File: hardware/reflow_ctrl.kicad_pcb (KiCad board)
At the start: 2 copper layers, 160 x 100 mm, 36 parts, among them IC1 MAX6675, IC2 ATXMEGA128A4U-A, P1 PDI, U1 LT1129CST-3.3, U2 MOC3063, U3 BTA41/600B, X1 USB-Mini-B, X2 Mains, X3 Load, X4 Thermocouple

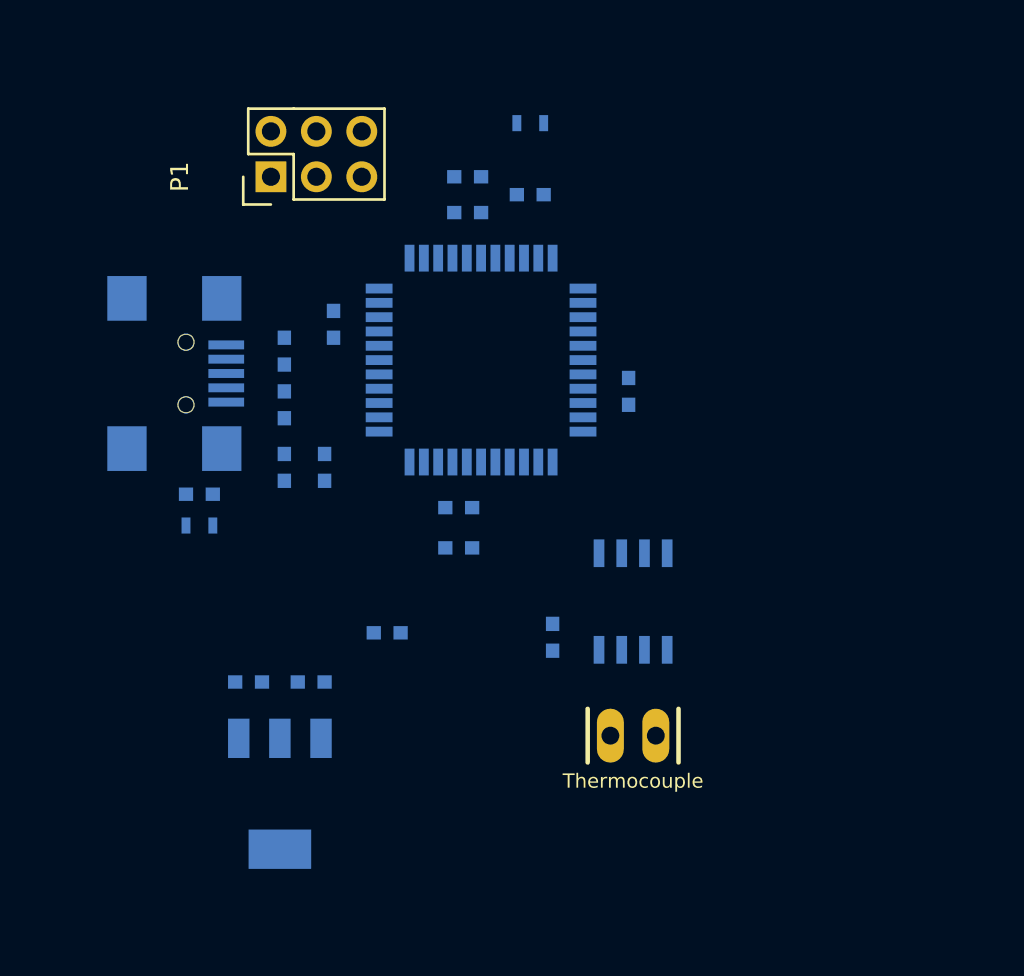
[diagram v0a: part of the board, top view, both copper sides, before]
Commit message: Use big USB-B THT connector
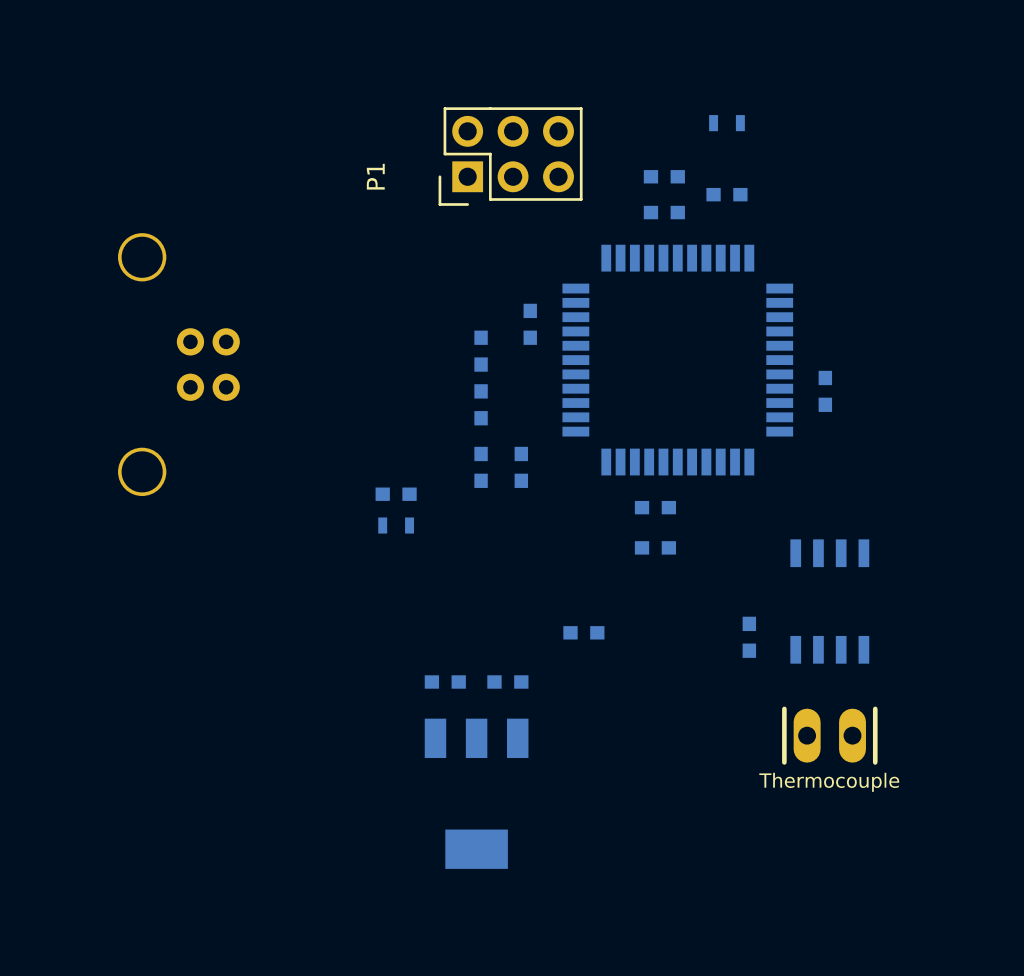
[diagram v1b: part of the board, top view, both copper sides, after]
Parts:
- X1: footprint uMIDI:USB-mini-B-UX60MB-5ST -> Connect:USB_B
- moved C1 11.0 mm to (82.5, 107.2)
- moved C10 11.0 mm to (97.5, 89.5)
- moved C11 11.0 mm to (102.2, 115.2)
- moved C2 11.0 mm to (85.2, 117.8)
- moved C3 11.0 mm to (89.5, 105.8)
- moved C4 11.0 mm to (97.0, 110.2)
- moved C5 11.0 mm to (88.8, 117.8)
- moved C6 11.0 mm to (106.5, 101.5)
- moved C7 11.0 mm to (97.0, 108.0)
- moved C8 11.0 mm to (90.0, 97.8)
- moved C9 11.0 mm to (97.5, 91.5)
- moved D1 11.0 mm to (87.2, 105.8)
- moved D2 11.0 mm to (87.2, 99.2)
- moved D3 11.0 mm to (87.2, 102.2)
- moved IC1 11.0 mm to (106.8, 113.2)
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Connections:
- net Net-(D2-Pad2) renamed /USB_n
- net Net-(D3-Pad2) renamed /USB_p
- X1 pad 4: (no net) -> GND
- X1 pad 5: GND -> Net-(C1-Pad1)

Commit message: Update board
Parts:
- removed C10, C4, C5, L1: 10u, Capacitors_SMD:C_0603
- removed C3, C6, C7, C8, C9: 100n, Capacitors_SMD:C_0603
- removed D1, D2, D3: TVS 5V, Capacitors_SMD:C_0603
- removed IC2: ATXMEGA128A4U-A, Housings_QFP:TQFP-44_10x10mm_Pitch0.8mm
- removed L2: Bead 1k@100MHz, Capacitors_SMD:C_0603
- removed P1: PDI, Pin_Headers:Pin_Header_Straight_2x03
- removed R1: 1M, Resistors_SMD:R_0603
- removed R2: 10k, Resistors_SMD:R_0603
- removed REF**: EuroBoard160mmX100mm_holes, EuroBoard_Outline:EuroBoard160mmX100mm_holes
- removed U1: LT1129CST-3.3, uMIDI:SOT-223
- C1: value 4.7n -> 100n
- C2: value 10u -> 100n
- X1: value USB-Mini-B -> Master; footprint Connect:USB_B -> uMIDI:Con-boxed_header-THT; moved to F.Cu
- moved X4 63.4 mm to (125.0, 60.0), turned to 180 degrees
- moved IC1 46.9 mm to (125.0, 70.0), turned to 270 degrees
- moved X1 36.9 mm to (108.7, 89.5), turned to 90 degrees
- moved C1 24.3 mm to (106.5, 111.2)
- moved C2 24.3 mm to (109.2, 121.8)
- moved X3 24.3 mm to (190.0, 75.0)
- moved X2 23.6 mm to (190.0, 100.0)
- moved F1 22.9 mm to (165.0, 112.5)
- moved C12 22.4 mm to (160.0, 77.8)
- moved R3 22.4 mm to (149.2, 100.8)
- moved R4 22.4 mm to (149.8, 82.0)
- moved R5 22.4 mm to (145.5, 71.0)
- moved R6 22.4 mm to (160.0, 83.0)
- moved U2 22.4 mm to (146.8, 91.5)
- moved U3 22.4 mm to (149.8, 76.2)
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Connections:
- C1 pad 1: Net-(C1-Pad1) -> +3V3
- C11 pad 1: +5V -> +3V3
- C2 pad 1: VBUS -> +3V3
- IC1 pad 4: +5V -> +3V3
- X1 pad 1: VBUS -> +3V3
- X1 pad 2: /USB_p -> (no net)
- X1 pad 3: /USB_n -> (no net)
- X1 pad 4: GND -> (no net)
- X1 pad 5: Net-(C1-Pad1) -> /TC_SO
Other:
- board outline removed

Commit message: Prepare net classes
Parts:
- moved F1 17.5 mm to (172.0, 96.5), turned to 270 degrees
- moved VR1 16.0 mm to (172.8, 72.0)
- moved C12 14.3 mm to (165.5, 64.5)
- moved R6 13.7 mm to (165.5, 70.5)
- moved X3 5.00 mm to (190.0, 70.0)
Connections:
- net Net-(C12-Pad1) renamed /Snub
- net Net-(F1-Pad1) renamed /L_main_fused
- net Net-(R4-Pad2) renamed /MOC_A1
- net Net-(R5-Pad1) renamed /MOC_A2
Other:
- net class AC added: clearance 1, trace_width 5, via_dia 1.5, via_drill 1
- net class AC-LC added: clearance 1, trace_width 0.3, via_dia 1.5, via_drill 1
- net class Default: clearance 0.2 -> 0.3; trace_width 0.25 -> 0.3; via_dia 0.6 -> 1.5; via_drill 0.4 -> 1
- rule trace_clearance: 0.2 -> 0.3

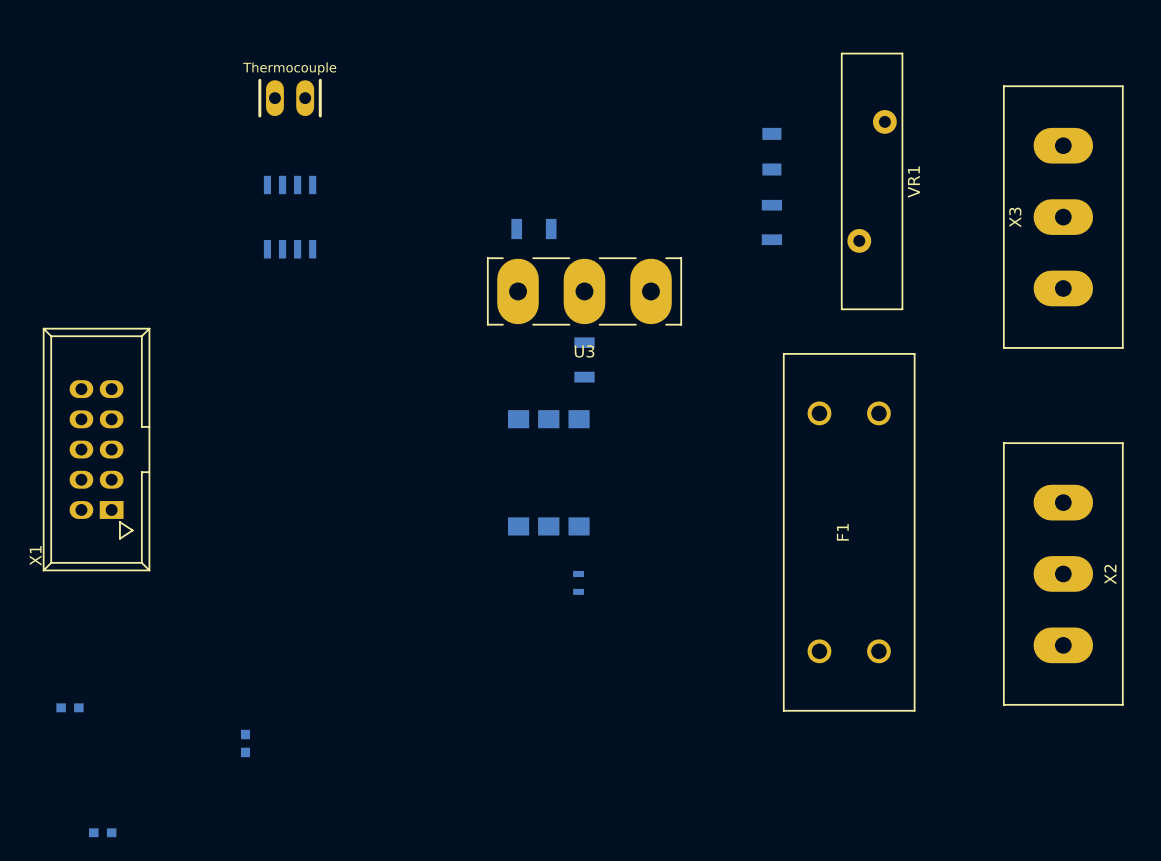
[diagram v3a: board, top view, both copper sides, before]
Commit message: Add mounting holes
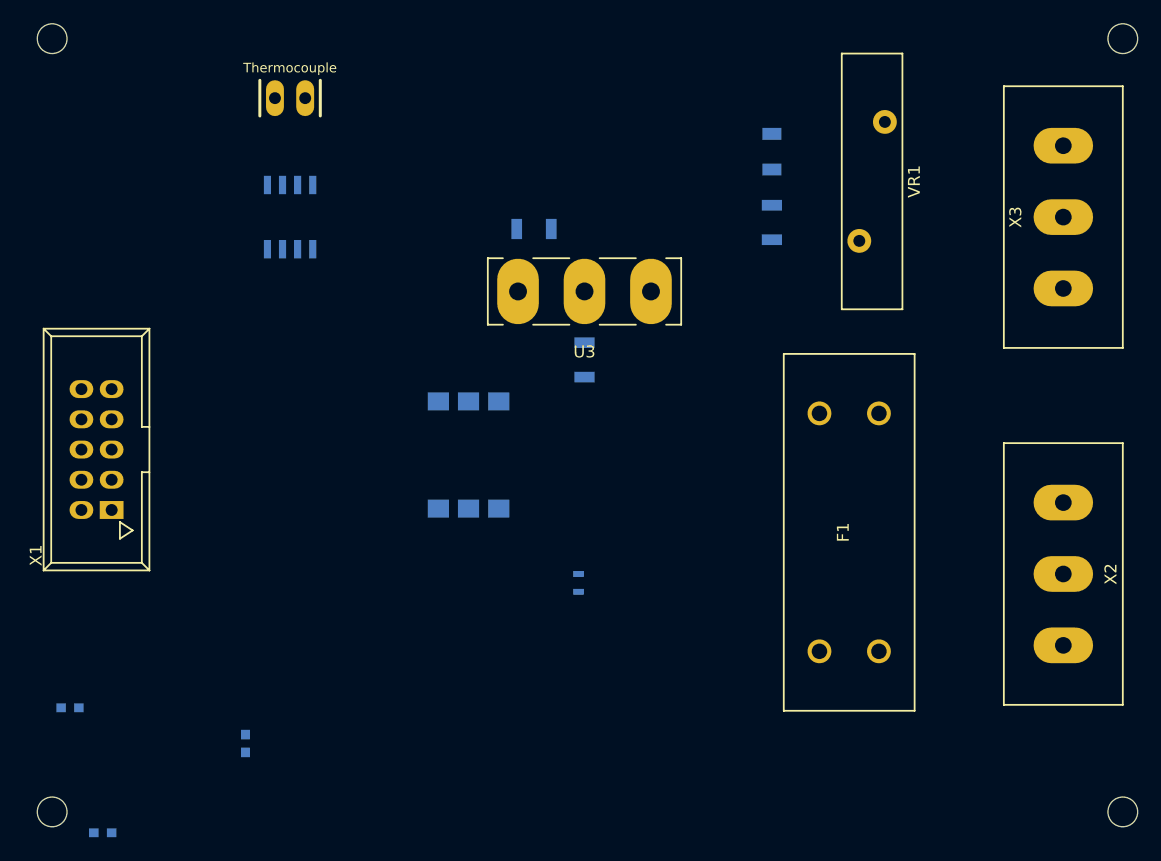
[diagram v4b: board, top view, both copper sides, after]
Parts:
- added REF**: MountingHole_2-5mm, Mounting_Holes:MountingHole_2-5mm, F.Cu at (195.0, 120.0)
- added REF**: MountingHole_2-5mm, Mounting_Holes:MountingHole_2-5mm, F.Cu at (105.0, 120.0)
- added REF**: MountingHole_2-5mm, Mounting_Holes:MountingHole_2-5mm, F.Cu at (105.0, 55.0)
- added REF**: MountingHole_2-5mm, Mounting_Holes:MountingHole_2-5mm, F.Cu at (195.0, 55.0)
- moved U2 6.91 mm to (140.0, 90.0)
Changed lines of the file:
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@@
 (kicad_pcb (version 4) (host pcbnew "(2015-09-12 BZR 6188)-product")
   (general
-    (links 33)
+    (links 0)
     (no_connects 33)
-    (area 99.899999 49.899999 200.100001 125.425)
+    (area 95.615476 49.075 213 132.700001)
     (thickness 1.6)
-    (drawings 4)
+    (drawings 6)
     (tracks 0)
     (zones 0)
-    (modules 17)
+    (modules 21)
     (nets 18)
   )
@@
     (add_net /Snub)
   )
+  (module Mounting_Holes:MountingHole_2-5mm (layer F.Cu)
+    (at 195 120)
+    (descr "Mounting hole, Befestigungsbohrung, 2,5mm, No Annular, Kein Restring,")
+    (tags "Mounting hole, Befestigungsbohrung, 2,5mm, No Annular, Kein Restring,")
+    (fp_text reference REF** (at 0 -3.50012) (layer F.SilkS) hide
+      (effects (font (size 1 1) (thickness 0.15)))
+    )
+    (fp_text value MountingHole_2-5mm (at 0 4) (layer F.Fab)
+      (effects (font (size 1 1) (thickness 0.15)))
+    )
+    (fp_circle (center 0 0) (end 2.5 0) (layer Cmts.User) (width 0.381))
+    (pad 1 thru_hole circle (at 0 0) (size 2.5 2.5) (drill 2.5) (layers))
+  )
+  (module Mounting_Holes:MountingHole_2-5mm (layer F.Cu)
+    (at 105 120)
+    (descr "Mounting hole, Befestigungsbohrung, 2,5mm, No Annular, Kein Restring,")
+    (tags "Mounting hole, Befestigungsbohrung, 2,5mm, No Annular, Kein Restring,")
+    (fp_text reference REF** (at 0 -3.50012) (layer F.SilkS) hide
+      (effects (font (size 1 1) (thickness 0.15)))
+    )
+    (fp_text value MountingHole_2-5mm (at 0 4) (layer F.Fab)
+      (effects (font (size 1 1) (thickness 0.15)))
+    )
+    (fp_circle (center 0 0) (end 2.5 0) (layer Cmts.User) (width 0.381))
+    (pad 1 thru_hole circle (at 0 0) (size 2.5 2.5) (drill 2.5) (layers))
+  )
+  (module Mounting_Holes:MountingHole_2-5mm (layer F.Cu)
+    (at 105 55)
+    (descr "Mounting hole, Befestigungsbohrung, 2,5mm, No Annular, Kein Restring,")
+    (tags "Mounting hole, Befestigungsbohrung, 2,5mm, No Annular, Kein Restring,")
+    (fp_text reference REF** (at 0 -3.50012) (layer F.SilkS) hide
+      (effects (font (size 1 1) (thickness 0.15)))
+    )
+    (fp_text value MountingHole_2-5mm (at 0 -4) (layer F.Fab)
+      (effects (font (size 1 1) (thickness 0.15)))
+    )
+    (fp_circle (center 0 0) (end 2.5 0) (layer Cmts.User) (width 0.381))
+    (pad 1 thru_hole circle (at 0 0) (size 2.5 2.5) (drill 2.5) (layers))
+  )
   (module Capacitors_SMD:C_0603 (layer B.Cu)
     (at 106.5 111.25 180)
@@
   )
   (module uMIDI:MOC3063_SMT (layer B.Cu)
-    (at 146.75 91.5 180)
+    (at 140 90 180)
     (fp_text reference U2 (at 0 -7 180) (layer B.SilkS)
       (effects (font (size 1 1) (thickness 0.15)) (justify mirror))
@@
       (net 1 GND))
   )
+  (module Mounting_Holes:MountingHole_2-5mm (layer F.Cu)
+    (at 195 55)
+    (descr "Mounting hole, Befestigungsbohrung, 2,5mm, No Annular, Kein Restring,")
+    (tags "Mounting hole, Befestigungsbohrung, 2,5mm, No Annular, Kein Restring,")
+    (fp_text reference REF** (at 0 -3.50012) (layer F.SilkS) hide
+      (effects (font (size 1 1) (thickness 0.15)))
+    )
+    (fp_text value MountingHole_2-5mm (at 0 -4) (layer F.Fab)
+      (effects (font (size 1 1) (thickness 0.15)))
+    )
+    (fp_circle (center 0 0) (end 2.5 0) (layer Cmts.User) (width 0.381))
+    (pad 1 thru_hole circle (at 0 0) (size 2.5 2.5) (drill 2.5) (layers))
+  )
+  (dimension 75 (width 0.3) (layer Dwgs.User)
+    (gr_text "75.000 mm" (at 206.35 87.5 90) (layer Dwgs.User)
+      (effects (font (size 1.5 1.5) (thickness 0.3)))
+    )
+    (feature1 (pts (xy 200 50) (xy 207.7 50)))
+    (feature2 (pts (xy 200 125) (xy 207.7 125)))
+    (crossbar (pts (xy 205 125) (xy 205 50)))
+    (arrow1a (pts (xy 205 50) (xy 205.586421 51.126504)))
+    (arrow1b (pts (xy 205 50) (xy 204.413579 51.126504)))
+    (arrow2a (pts (xy 205 125) (xy 205.586421 123.873496)))
+    (arrow2b (pts (xy 205 125) (xy 204.413579 123.873496)))
+  )
+  (dimension 100 (width 0.3) (layer Dwgs.User)
+    (gr_text "100.000 mm" (at 150 131.35) (layer Dwgs.User)
+      (effects (font (size 1.5 1.5) (thickness 0.3)))
+    )
+    (feature1 (pts (xy 200 125) (xy 200 132.7)))
+    (feature2 (pts (xy 100 125) (xy 100 132.7)))
+    (crossbar (pts (xy 100 130) (xy 200 130)))
+    (arrow1a (pts (xy 200 130) (xy 198.873496 130.586421)))
+    (arrow1b (pts (xy 200 130) (xy 198.873496 129.413579)))
+    (arrow2a (pts (xy 100 130) (xy 101.126504 130.586421)))
+    (arrow2b (pts (xy 100 130) (xy 101.126504 129.413579)))
+  )
   (gr_line (start 100 125) (end 100 50) (layer Margin) (width 0.2))

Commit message: Disentangle connector pinout; Start placement
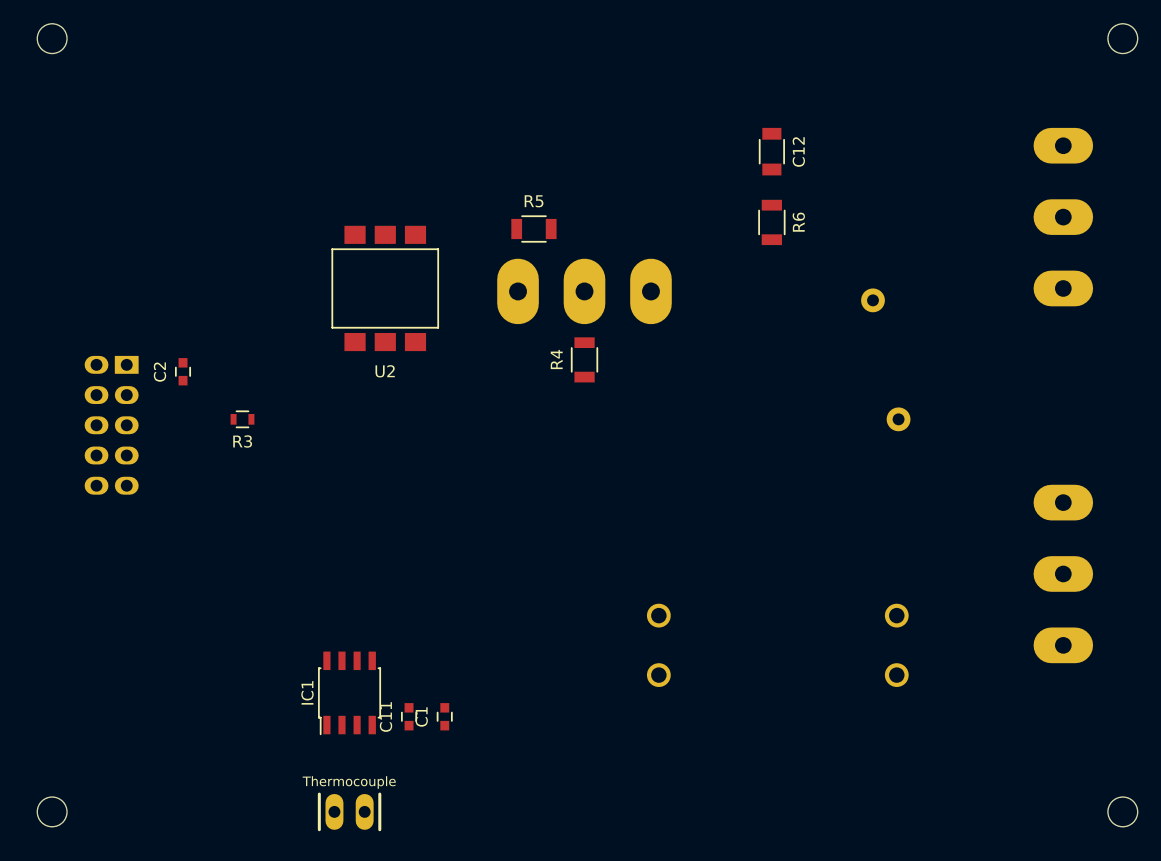
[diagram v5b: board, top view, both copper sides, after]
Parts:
- C1, C11, C12, C2, IC1, R3, R4, R5, R6, U2: moved to F.Cu
- F1, U3, VR1, X1, X2, X3: moved to B.Cu
- moved X4 60.2 mm to (130.0, 120.0)
- moved IC1 40.3 mm to (130.0, 110.0), turned to 90 degrees
- moved C2 39.3 mm to (116.0, 83.0), turned to 90 degrees
- moved C1 31.5 mm to (138.0, 112.0), turned to 90 degrees
- moved R3 31.4 mm to (121.0, 87.0), turned to 180 degrees
- moved U2 15.7 mm to (133.0, 76.0), turned to 0 degrees
- moved VR1 15.4 mm to (176.2, 87.0)
- moved C11 13.9 mm to (135.0, 112.0)
- moved F1 11.2 mm to (166.0, 106.0), turned to 0 degrees
- moved X1 2.40 mm to (110.0, 87.5), turned to 270 degrees
- turned C12 to 270 degrees
- turned R4 to 90 degrees
- turned R6 to 270 degrees
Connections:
- X1 pad 3: (no net) -> /PWR
- X1 pad 5: /TC_SO -> /TC_SCK
- X1 pad 8: /PWR -> (no net)
- X1 pad 9: /TC_SCK -> /TC_SO
